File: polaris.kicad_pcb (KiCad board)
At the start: 4 copper layers, 75 x 155 mm, 158 parts, among them J101 XT60-M, J102 SPI, J103 I2C, J104 PB, J105 SWD, J106 PYRO5, J107 PYRO4, J108 PYRO3, J109 PYRO2, J110 PYRO1, J111 PYRO0, J112 SERVO0, J113 SERVO1, J114 SERVO2, J115 SERVO3, J116 SERVO4, J117 SERVO5, J118 RADIO, J119 POWER, J301 USB_C_Receptacle_USB2.0_16P, J401 GNSS, J501 XT60-M, Q201 IRLZ44N, Q202 IRLZ44N, Q401 Q_NMOS, Q501 IRLZ44N, Q502 IRLZ44N, Q503 IRLZ44N, Q504 IRLZ44N, Q505 IRLZ44N, Q506 IRLZ44N, SW401 SW_Push, SW402 SW_Push, U1101 THD-2528-11SD-GF, U1201 W25Q128JVE, U201 BQ24005, U202 LM74700, U203 LM74700, U204 TLV75733PDBV, U205 LMR51430, U206 TPS7A2033PDBVR, U301 USBLC6-2SC6, U302 CH224K, U303 USBLC6-2SC6, U401 STM32F446VETx, U501 PC817, U502 PC817, U503 CD4051B, U504 PC817, U505 PC817, U506 PC817, U507 PC817, U601 ICM-42688-P, U701 LSM6DSO32TR, U801 MS5607, U901 LPS22HH, Y401 YXC YSX321SL

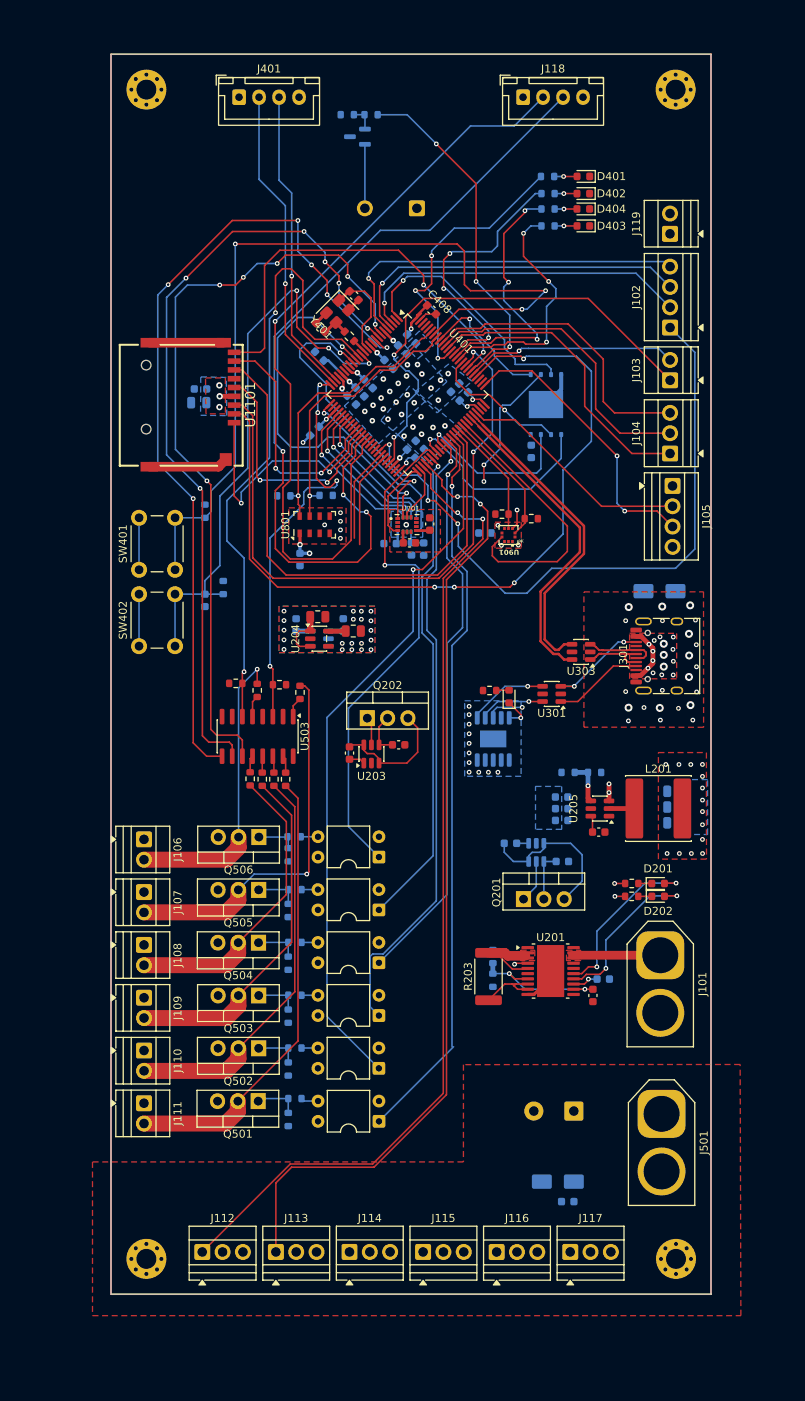
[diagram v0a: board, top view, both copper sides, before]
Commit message: Completed laying traces for PCB
Will begin resolving design rule issues later
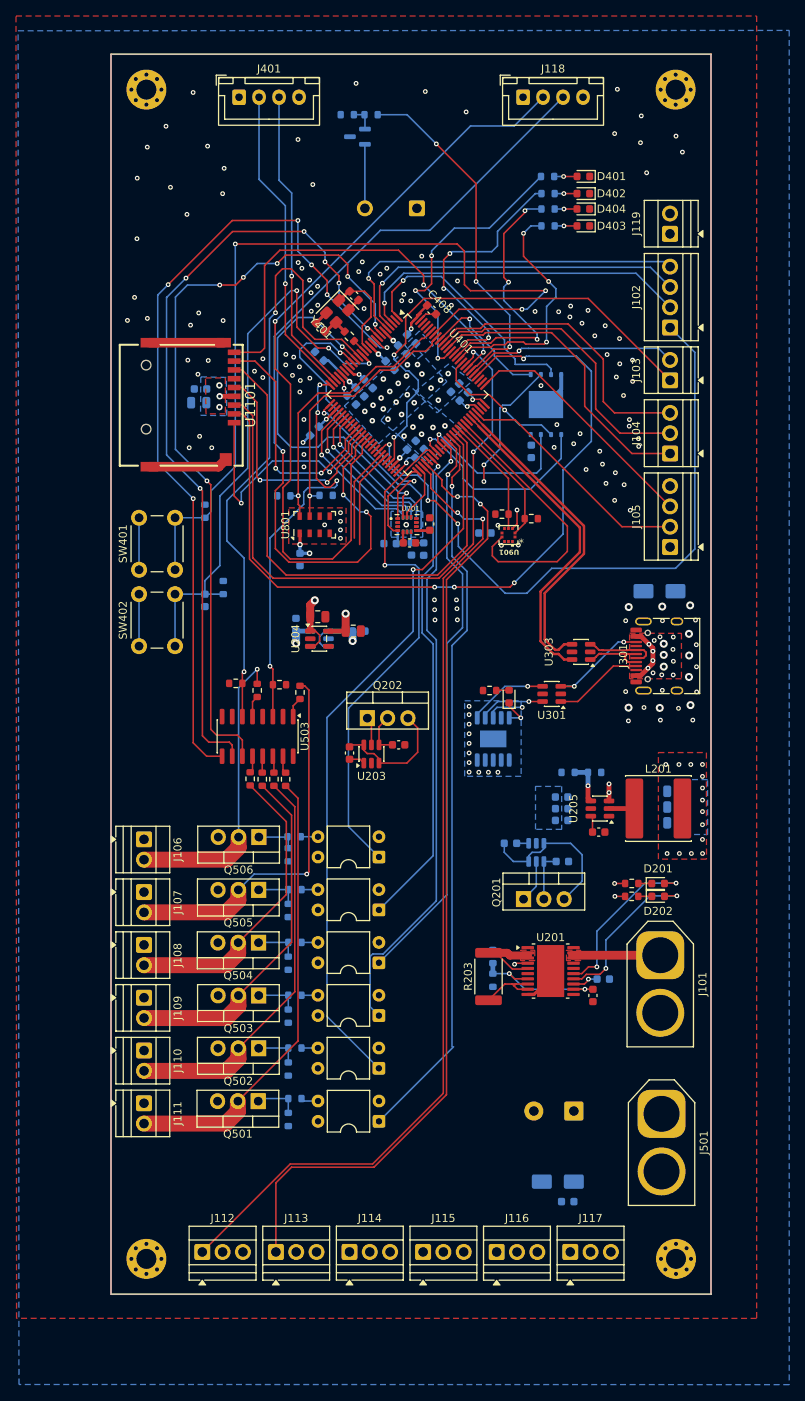
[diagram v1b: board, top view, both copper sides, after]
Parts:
- moved J105 7.65 mm to (156.9, 86.6), turned to 90 degrees
- moved C213 2.09 mm to (118.0, 97.1), turned to 0 degrees
- moved C416 0.20 mm to (121.9, 63.9)
- moved C216 0.05 mm to (110.1, 96.3)
- turned R901 to 0 degrees
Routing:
- net +3.3VA: track 1.77 -> 82.3 mm, vias 0 -> 1
- net +5V: track 8.59 -> 15.4 mm, vias 14 -> 16
- net /3_NavigationProcessor/SYS_SWCLK: track 35.7 -> 31.2 mm, vias 2 -> 0
- net +3.3V: track 55.7 -> 58.1 mm, vias 16 -> 17
- net /1_Power/IN: track 11.5 -> 9.91 mm
- net /3_NavigationProcessor/SYS_SWDIO: track 29.4 -> 30.1 mm
- net GND: vias 91 -> 175
- added copper zone on In2.Cu, net +3.3V
- added copper zone on In2.Cu, net /1_Power/USB_VCC
- added copper zone on In2.Cu, net /4_Pyrochannels/SERVO_PWR
- removed copper zone on F.Cu, net /4_Pyrochannels/SERVO_PWR

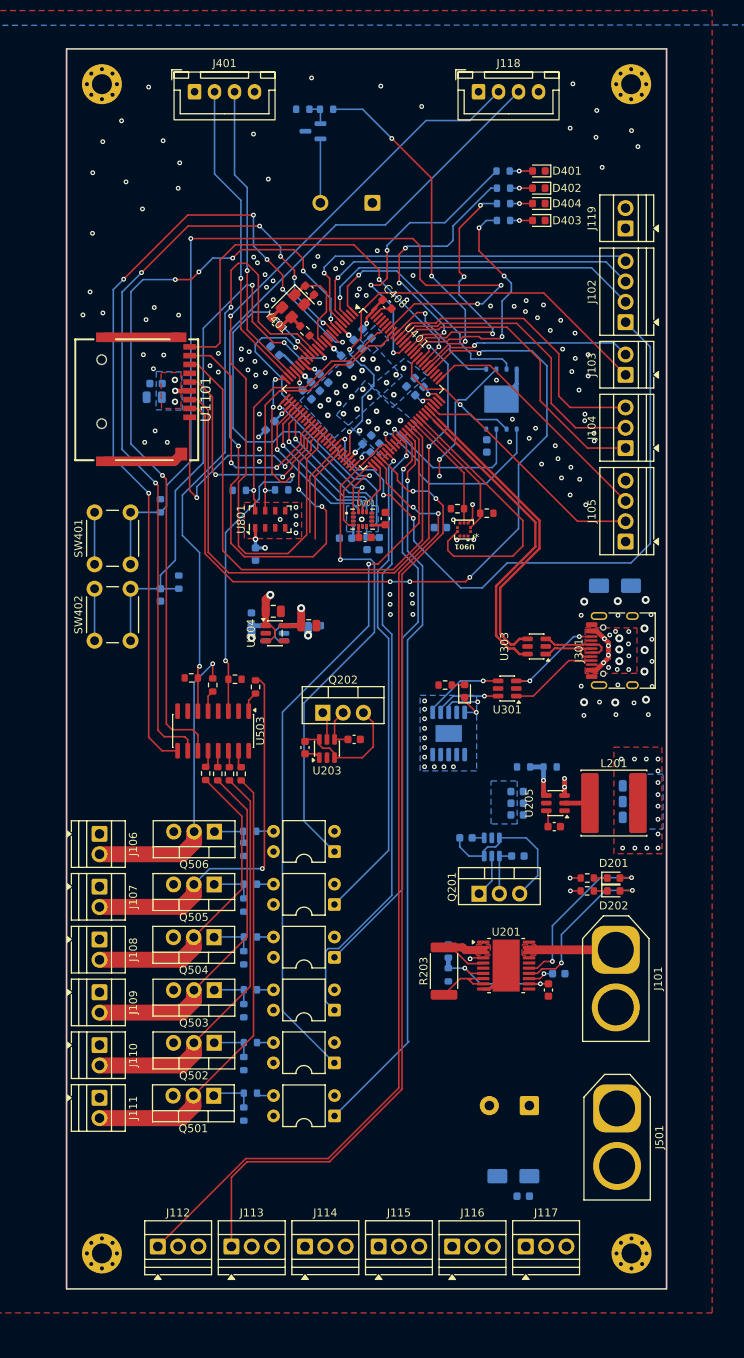
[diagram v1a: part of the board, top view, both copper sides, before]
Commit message: Resolved some DRC violations
Updated footprint for LPS22HH since the courtyard drawings were
causing issues
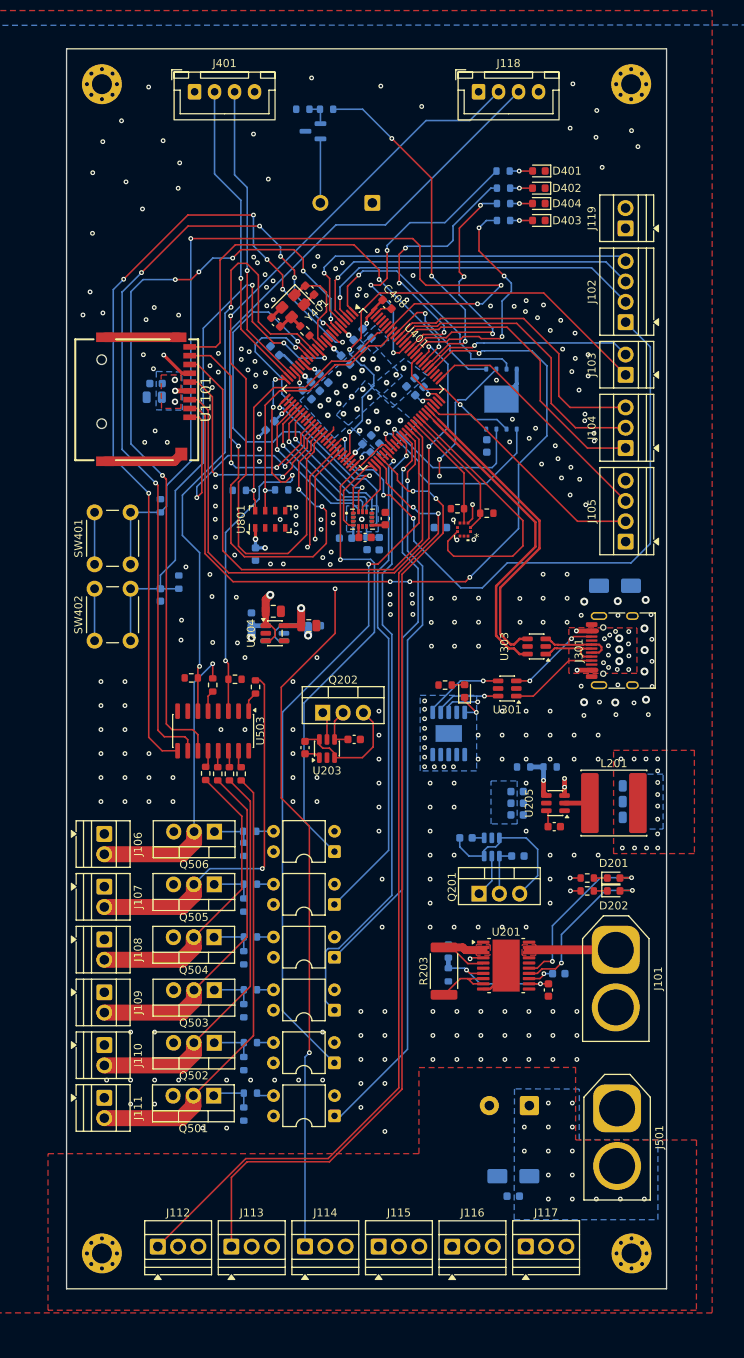
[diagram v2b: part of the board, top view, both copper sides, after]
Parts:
- moved C502 1.25 mm to (142.8, 168.4)
- moved J107 0.60 mm to (91.7, 129.7)
- moved J106 0.60 mm to (91.7, 123.1)
- moved J108 0.60 mm to (91.7, 136.3)
- moved J109 0.60 mm to (91.7, 142.9)
- moved J110 0.60 mm to (91.7, 149.5)
- moved J111 0.60 mm to (91.7, 156.1)
- turned R902 to 180 degrees
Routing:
- net +5V: track 15.4 -> 262.2 mm
- net /3_NavigationProcessor/SERVO_S2: track 0.00 -> 88.5 mm, vias 0 -> 2
- net GND: track 44.6 -> 48.9 mm, vias 175 -> 334
- net /1_Power/USB_VCC: track 37.5 -> 35.0 mm, vias 17 -> 19
- net /3_NavigationProcessor/SERVO_S4: track 11.8 -> 13.7 mm, vias 0 -> 1
- net /3_NavigationProcessor/SD_DAT2: track 31.5 -> 32.7 mm
- net /2_USB/USBC_CC2: track 12.9 -> 11.8 mm
- net /4_Pyrochannels/PYRO_0: track 59.0 -> 58.4 mm
- net /4_Pyrochannels/PYRO_3: track 39.8 -> 39.2 mm
- net /4_Pyrochannels/PYRO_2: track 46.2 -> 45.7 mm
- net /4_Pyrochannels/PYRO_4: track 50.0 -> 49.5 mm
- net /4_Pyrochannels/PYRO_1: track 52.6 -> 52.0 mm
- net /4_Pyrochannels/PYRO_5: track 40.1 -> 39.6 mm
- net /4_Pyrochannels/SERVO_PWR: vias 0 -> 15
- net /3_NavigationProcessor/SERVO_S5: vias 0 -> 1
- added copper zone on In2.Cu, net +5V
- added copper zone on B.Cu, net /4_Pyrochannels/SERVO_PWR
- added copper zone on F.Cu, net /4_Pyrochannels/SERVO_PWR
- added copper zone on In2.Cu, net GND
- removed copper zone on In2.Cu, net /4_Pyrochannels/SERVO_PWR
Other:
- board text removed: "U901"

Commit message: Major changes
Updated schematic for better power delivery
Changed 3.3V supply to buck converter instead of LDO due to heat
Deleted the entire PCB, redoing the whole thing due to problems in
laying traces that made some connections impossible to make
Also updated README to reflect these changes
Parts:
- removed C211: 10u, Capacitor_SMD:C_0805_2012Metric
- removed U206: TPS7A2033PDBVR, Package_TO_SOT_SMD:SOT-23-5
- added C218: 10u, Capacitor_SMD:C_0805_2012Metric, B.Cu at (100.5, 92.0)
- added C219: 22u, Capacitor_SMD:C_0805_2012Metric, B.Cu at (100.5, 95.0)
- added C220: 10u, Capacitor_SMD:C_0805_2012Metric, B.Cu at (100.5, 98.0)
- added FB402: FerriteBead, Inductor_SMD:L_0603_1608Metric, F.Cu at (92.2, 73.0)
- added L202: 4u7, Inductor_SMD:L_Sunlord_SWPA8040S, B.Cu at (93.5, 95.2)
- added R208: 100k, Resistor_SMD:R_0603_1608Metric, B.Cu at (86.6, 99.3)
- added R209: 22.1k, Resistor_SMD:R_0603_1608Metric, B.Cu at (86.6, 101.8)
- BZ401, C1101, C1102, C1201, C202, C203, C205, C403, C404, C405, C406, C407, C409, C410, C411, C412, C413, C414, C415, C416, C501, C502, C601, C602, C603, C801, C901, D301, D501, Q401, R201, R202, R401, R402, R406, R407, R801, R802, U1201, U202, U302, U601: moved to F.Cu
- C208: value 10u -> 3u3; footprint Capacitor_SMD:C_0805_2012Metric -> Capacitor_SMD:C_0603_1608Metric; moved to B.Cu
- C212, L201, U205, U701: moved to B.Cu
- C213, C216: value 1u -> 100n
- J106: value PYRO5 -> PYRO0
- J107: value PYRO4 -> PYRO1
- J108: value PYRO3 -> PYRO2
- J109: value PYRO2 -> PYRO3
- J110: value PYRO1 -> PYRO4
- J111: value PYRO0 -> PYRO5
- SW401, SW402: footprint Button_Switch_THT:SW_PUSH_6mm -> Button_Switch_SMD:SW_SPST_TS-1088-xR020
- U204: value TLV75733PDBV -> LMR51430; footprint Package_TO_SOT_SMD:SOT-23-5 -> Package_TO_SOT_SMD:SOT-23-6; moved to B.Cu
- moved J119 253.3 mm to (-95.4, 24.8), turned to 0 degrees
- moved C201 237.2 mm to (-51.4, 13.1), turned to 0 degrees
- moved C202 235.8 mm to (-51.4, 15.6)
- moved D201 231.2 mm to (-56.6, 36.2)
- moved D202 230.8 mm to (-56.6, 38.8)
- moved R204 227.1 mm to (-43.4, 13.1), turned to 0 degrees
- moved R205 226.7 mm to (-43.4, 15.6), turned to 0 degrees
- moved U202 225.2 mm to (-56.0, 14.2), turned to 0 degrees
- moved C205 220.3 mm to (-51.4, 23.1)
- moved C203 215.9 mm to (-51.4, 18.1)
- moved R202 214.2 mm to (-47.4, 28.1), turned to 0 degrees
- moved R201 213.9 mm to (-47.4, 25.6), turned to 0 degrees
- moved R203 204.3 mm to (-32.6, 22.3), turned to 0 degrees
- moved Q201 203.0 mm to (-38.2, 30.8)
- moved R505 200.8 mm to (-88.9, 80.5), turned to 0 degrees
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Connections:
- net /2_USB/USBC_CC1 renamed /2_USB/CONN_CC1
- net /2_USB/USBC_CC2 renamed /2_USB/CONN_CC2
- net /2_USB/USB_CC1 renamed /2_USB/CC1
- net /2_USB/USB_CC2 renamed /2_USB/CC2
- net /2_USB/USB_D+ renamed /2_USB/USB_D+_
- C208 pad 1: +5V -> POWER
- C213 pad 1: +5V -> POWER
- C216 pad 1: +3.3VA -> /1_Power/C_BOOT
- C216 pad 2: GND -> /1_Power/REG_SW
- J106 pad 2: /4_Pyrochannels/PYRO_5 -> /4_Pyrochannels/PYRO_0
- J107 pad 2: /4_Pyrochannels/PYRO_4 -> /4_Pyrochannels/PYRO_1
- J108 pad 2: /4_Pyrochannels/PYRO_3 -> /4_Pyrochannels/PYRO_2
- J109 pad 2: /4_Pyrochannels/PYRO_2 -> /4_Pyrochannels/PYRO_3
- J110 pad 2: /4_Pyrochannels/PYRO_1 -> /4_Pyrochannels/PYRO_4
- J111 pad 2: /4_Pyrochannels/PYRO_0 -> /4_Pyrochannels/PYRO_5
- J401 pad 4: +3.3VA -> +3.3V
- R505 pad 2: /4_Pyrochannels/PYRO_0 -> /4_Pyrochannels/PYRO_C0
- R506 pad 2: /4_Pyrochannels/PYRO_1 -> /4_Pyrochannels/PYRO_C1
- R513 pad 2: /4_Pyrochannels/PYRO_2 -> /4_Pyrochannels/PYRO_C2
- R514 pad 2: /4_Pyrochannels/PYRO_3 -> /4_Pyrochannels/PYRO_C3
- R519 pad 2: /4_Pyrochannels/PYRO_4 -> /4_Pyrochannels/PYRO_C4
- R520 pad 2: /4_Pyrochannels/PYRO_5 -> /4_Pyrochannels/PYRO_C5
- U204 pad 1: +5V -> GND
- U204 pad 2: GND -> /1_Power/REG_SW
- U204 pad 3: +5V -> POWER
- U204 pad 4: unconnected-(U204-NC-Pad4) -> /1_Power/FB
- U204 pad 5: +3.3V -> POWER
- U401 pad 22: +3.3V -> Net-(U401-VDDA)
- U503 pad 1: /4_Pyrochannels/PYRO_4 -> /4_Pyrochannels/PYRO_C4
- U503 pad 12: /4_Pyrochannels/PYRO_3 -> /4_Pyrochannels/PYRO_C3
- U503 pad 13: /4_Pyrochannels/PYRO_2 -> /4_Pyrochannels/PYRO_C2
- U503 pad 14: /4_Pyrochannels/PYRO_1 -> /4_Pyrochannels/PYRO_C1
- U503 pad 15: /4_Pyrochannels/PYRO_0 -> /4_Pyrochannels/PYRO_C0
- U503 pad 5: /4_Pyrochannels/PYRO_5 -> /4_Pyrochannels/PYRO_C5
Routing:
- net +5V: track 262.2 -> 0.00 mm, vias 16 -> 0
- net /3_NavigationProcessor/SERVO_S0: track 123.4 -> 0.00 mm, vias 2 -> 0
- net /3_NavigationProcessor/SERVO_S1: track 120.3 -> 0.00 mm, vias 2 -> 0
- net /3_NavigationProcessor/MUX_C: track 106.4 -> 0.00 mm, vias 6 -> 0
- net /3_NavigationProcessor/RF_RX: track 106.0 -> 0.00 mm, vias 3 -> 0
- net Net-(U401-BOOT0): track 105.9 -> 0.00 mm, vias 3 -> 0
- net /3_NavigationProcessor/SD_DAT3: track 101.2 -> 0.00 mm, vias 4 -> 0
- net /3_NavigationProcessor/MUX_B: track 100.0 -> 0.00 mm, vias 6 -> 0
- net /3_NavigationProcessor/RF_TX: track 98.2 -> 0.00 mm, vias 1 -> 0
- net /3_NavigationProcessor/MUX_A: track 97.0 -> 0.00 mm, vias 6 -> 0
- net /3_NavigationProcessor/PYRO_0: track 92.1 -> 0.00 mm, vias 1 -> 0
- net /3_NavigationProcessor/PYRO_1: track 90.1 -> 0.00 mm, vias 1 -> 0
- net /3_NavigationProcessor/SERVO_S2: track 88.5 -> 0.00 mm, vias 2 -> 0
- net /3_NavigationProcessor/SPI4_SCK: track 82.9 -> 0.00 mm, vias 3 -> 0
- net +3.3VA: track 82.3 -> 0.00 mm, vias 1 -> 0
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- removed copper zone on B.Cu, net +3.3V
- removed copper zone on F.Cu, net +3.3V
- removed copper zone on In2.Cu, net +3.3V
- removed copper zone on B.Cu, net +5V
- removed copper zone on F.Cu, net +5V
- removed copper zone on In2.Cu, net +5V
- removed copper zone on F.Cu, net /1_Power/IN
- removed copper zone on F.Cu, net /1_Power/USB_VCC
- removed copper zone on In2.Cu, net /1_Power/USB_VCC
- removed copper zone on B.Cu, net /4_Pyrochannels/SERVO_PWR
- removed copper zone on F.Cu, net /4_Pyrochannels/SERVO_PWR
- removed copper zone on B.Cu, net GND
- removed copper zone on F.Cu, net GND
- removed copper zone on In1.Cu, net GND
- removed copper zone on In2.Cu, net GND
- removed copper zone on In2.Cu, net POWER
- removed copper zone on F.Cu, net VBAT_VIN

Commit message: Finished most of component re-placement
Began laying tracks for important connections
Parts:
- removed C220: 10u, Capacitor_SMD:C_0805_2012Metric
- removed R403: 0R, Resistor_SMD:R_0603_1608Metric
- added C211: 10u, Capacitor_SMD:C_0805_2012Metric, B.Cu at (86.0, 94.5)
- added R101: 0R, Resistor_SMD:R_0603_1608Metric, B.Cu at (88.0, 47.3)
- BZ401, C1101, C1102, C1201, C404, C413, C416, FB402, U301, U302, U601: moved to B.Cu
- C208: value 3u3 -> 4u7
- C219: value 22u -> 100n; footprint Capacitor_SMD:C_0805_2012Metric -> Capacitor_SMD:C_0603_1608Metric
- C401, C402: value 12p -> 20p
- L202: value 4u7 -> 10u
- U1201: value W25Q128JVE -> W25Q128JVS; footprint Package_SON:WSON-8-1EP_8x6mm_P1.27mm_EP3.4x4.3mm -> Package_SO:SOIC-8_5.3x5.3mm_P1.27mm
- U701: moved to F.Cu
- moved C407 201.4 mm to (128.5, 51.0)
- moved C1101 198.0 mm to (141.5, 68.0)
- moved C1102 193.5 mm to (141.3, 66.0)
- moved C406 189.2 mm to (120.0, 67.0), turned to -90 degrees
- moved J119 180.7 mm to (82.0, 59.0), turned to -90 degrees
- moved C404 180.1 mm to (110.2, 59.0)
- moved D302 177.0 mm to (145.7, 95.5)
- moved R301 177.0 mm to (149.7, 95.5), turned to 180 degrees
- moved D301 174.6 mm to (147.5, 79.0)
- moved C401 169.8 mm to (100.0, 53.0)
- moved C402 169.1 mm to (100.0, 59.0), turned to 180 degrees
- moved C403 168.9 mm to (99.7, 61.0), turned to 180 degrees
- moved U301 167.8 mm to (136.9, 92.0), turned to 180 degrees
- moved U302 167.4 mm to (129.4, 93.5)
- moved C901 162.4 mm to (126.0, 76.0), turned to 180 degrees
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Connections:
- net /2_USB/USB_D+_ renamed /2_USB/USB_D+
- C208 pad 1: POWER -> +5V
- C212 pad 1: /1_Power/C_BOOT -> /1_Power/5V_CBOOT
- C212 pad 2: /1_Power/REG_SW -> /1_Power/5V_SW
- C213 pad 1: POWER -> +5V
- C216 pad 1: /1_Power/C_BOOT -> /1_Power/3V3_CBOOT
- C216 pad 2: /1_Power/REG_SW -> /1_Power/3V3_SW
- C416 pad 1: +3.3V -> Net-(U401-VDDA)
- J102 pad 1: /3_NavigationProcessor/SPI4_SCK -> Net-(J102-Pin_1)
- L201 pad 1: /1_Power/REG_SW -> /1_Power/5V_SW
- L202 pad 1: /1_Power/REG_SW -> /1_Power/3V3_SW
- R206 pad 2: /1_Power/FB -> /1_Power/5V_FB
- R207 pad 1: /1_Power/FB -> /1_Power/5V_FB
- R208 pad 2: /1_Power/FB -> /1_Power/3V3_FB
- R209 pad 1: /1_Power/FB -> /1_Power/3V3_FB
- U204 pad 2: /1_Power/REG_SW -> /1_Power/3V3_SW
- U204 pad 3: POWER -> +5V
- U204 pad 4: /1_Power/FB -> /1_Power/3V3_FB
- U204 pad 5: POWER -> +5V
- U204 pad 6: /1_Power/C_BOOT -> /1_Power/3V3_CBOOT
- U205 pad 2: /1_Power/REG_SW -> /1_Power/5V_SW
- U205 pad 4: /1_Power/FB -> /1_Power/5V_FB
- U205 pad 6: /1_Power/C_BOOT -> /1_Power/5V_CBOOT
- U301 pad 1: /2_USB/CONN_CC1 -> /2_USB/CONN_CC2
- U301 pad 3: /2_USB/CONN_CC2 -> /2_USB/CONN_CC1
- U301 pad 4: /2_USB/CC2 -> /2_USB/CC1
- U301 pad 6: /2_USB/CC1 -> /2_USB/CC2
- U401 pad 13: Net-(U401-PH1) -> /3_NavigationProcessor/OSC_OUT
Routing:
- net /2_USB/USB_D-: track 0.00 -> 43.3 mm
- net /2_USB/USB_D+: track 0.00 -> 43.3 mm
- net /3_NavigationProcessor/SPI4_SCK: track 0.00 -> 39.2 mm, vias 0 -> 1
- net /3_NavigationProcessor/LPS_SCL: track 0.00 -> 35.2 mm, vias 0 -> 4
- net /3_NavigationProcessor/SYS_SWDIO: track 0.00 -> 34.8 mm, vias 0 -> 1
- net /3_NavigationProcessor/MS_SDA: track 0.00 -> 34.8 mm, vias 0 -> 2
- net /3_NavigationProcessor/MS_SCL: track 0.00 -> 33.9 mm, vias 0 -> 2
- net /3_NavigationProcessor/SYS_SWCLK: track 0.00 -> 33.7 mm, vias 0 -> 1
- net /3_NavigationProcessor/SD_CD: track 0.00 -> 33.4 mm, vias 0 -> 2
- net /3_NavigationProcessor/LPS_SDA: track 0.00 -> 32.2 mm, vias 0 -> 4
- net /3_NavigationProcessor/SD_DAT3: track 0.00 -> 31.2 mm, vias 0 -> 2
- net /3_NavigationProcessor/FLASH_IO2: track 0.00 -> 30.0 mm
- net +3.3V: track 0.00 -> 29.9 mm, vias 0 -> 1
- net /3_NavigationProcessor/SD_CMD: track 0.00 -> 28.6 mm, vias 0 -> 2
- net /3_NavigationProcessor/SPI4_MOSI: track 0.00 -> 26.6 mm
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- added copper zone on In1.Cu, net GND
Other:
- board text added: "VREF"
